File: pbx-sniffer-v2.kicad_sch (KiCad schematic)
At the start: 1 part

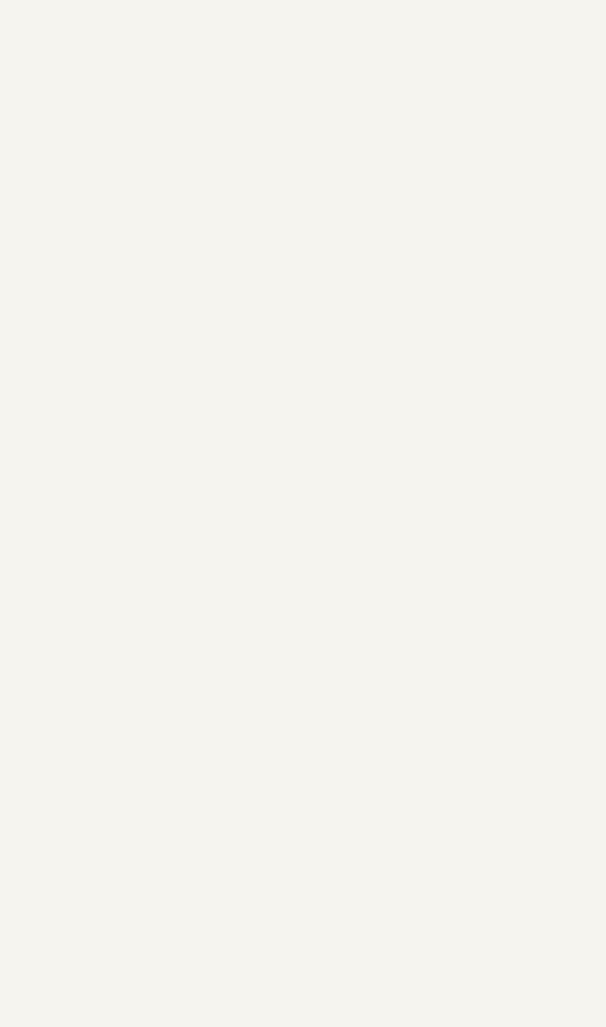
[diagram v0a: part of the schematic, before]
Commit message: first iteration of line control schematic
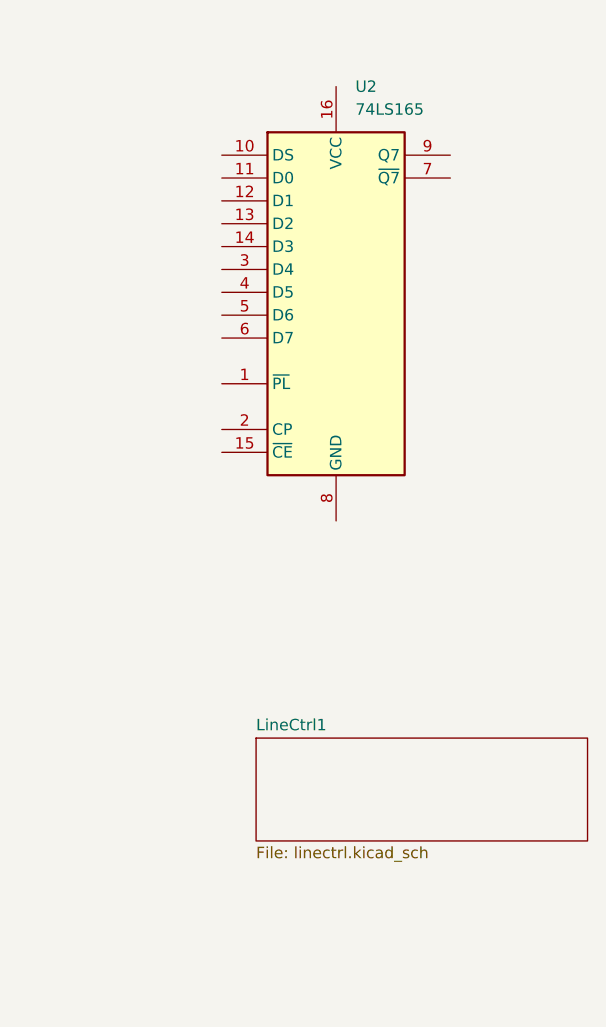
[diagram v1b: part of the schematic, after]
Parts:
- added U2: 74LS165, symbol 74xx:74LS165
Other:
- added sheet LineCtrl1 (linectrl.kicad_sch)
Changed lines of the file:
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@@
+	)
+	(symbol
+		(lib_id "74xx:74LS165")
+		(at 218.44 60.96 0)
+		(unit 1)
+		(body_style 1)
+		(exclude_from_sim no)
+		(in_bom yes)
+		(on_board yes)
+		(in_pos_files yes)
+		(dnp no)
+		(fields_autoplaced yes)
+		(property "Reference" "U2"
+			(at 220.5833 38.1 0)
+			(show_name no)
+			(do_not_autoplace no)
+			(effects
+				(font
+					(size 1.27 1.27)
+				)
+				(justify left)
+			)
+		)
+		(property "Value" "74LS165"
+			(at 220.5833 40.64 0)
+			(show_name no)
+			(do_not_autoplace no)
+			(effects
+				(font
+					(size 1.27 1.27)
+				)
+				(justify left)
+			)
+		)
+		(property "Footprint" ""
+			(at 218.44 60.96 0)
+			(hide yes)
+			(show_name no)
+			(do_not_autoplace no)
+			(effects
+				(font
+					(size 1.27 1.27)
+				)
+			)
+		)
+		(property "Datasheet" "https://www.ti.com/lit/ds/symlink/sn74ls165a.pdf"
+			(at 218.44 60.96 0)
+			(hide yes)
+			(show_name no)
+			(do_not_autoplace no)
+			(effects
+				(font
+					(size 1.27 1.27)
+				)
+			)
+		)
+		(property "Description" "Shift Register 8-bit, parallel load"
+			(at 218.44 60.96 0)
+			(hide yes)
+			(show_name no)
+			(do_not_autoplace no)
+			(effects
+				(font
+					(size 1.27 1.27)
+				)
+			)
+		)
+		(pin "14"
+		)
+		(pin "7"
+		)
+		(pin "3"
+		)
+		(pin "5"
+		)
+		(pin "8"
+		)
+		(pin "4"
+		)
+		(pin "2"
+		)
+		(pin "10"
+		)
+		(pin "6"
+		)
+		(pin "9"
+		)
+		(pin "1"
+		)
+		(pin "12"
+		)
+		(pin "11"
+		)
+		(pin "15"
+		)
+		(pin "16"
+		)
+		(pin "13"
+		)
+		(instances
+			(project "pbx-sniffer-v2"
+				(path "/eb421281-26a1-483f-b39a-0425ec8eb8df"
+					(reference "U2")
+					(unit 1)
+				)
+			)
+		)
 	)
 	(symbol
@@
 				)
 			)
+		)
+	)
+	(sheet
+		(at 209.55 110.49)
+		(size 36.83 11.43)
+		(exclude_from_sim no)
+		(in_bom yes)
+		(on_board yes)
+		(dnp no)
+		(fields_autoplaced yes)
+		(stroke
+			(width 0.1524)
+			(type solid)
+		)
+		(fill
+			(color 0 0 0 0)
+		)
+		(property "Sheetname" "LineCtrl1"
+			(at 209.55 109.7784 0)
+			(show_name no)
+			(do_not_autoplace no)
+			(effects
+				(font
+					(size 1.27 1.27)
+				)
+				(justify left bottom)
+			)
+		)
+		(property "Sheetfile" "linectrl.kicad_sch"
+			(at 209.55 122.5046 0)
+			(show_name no)
+			(do_not_autoplace no)
+			(effects
+				(font
+					(size 1.27 1.27)
+				)
+				(justify left top)
+			)
+		)
+		(instances
+			(project "pbx-sniffer-v2"
+				(path "/eb421281-26a1-483f-b39a-0425ec8eb8df"
+					(page "2")
+				)
+			)

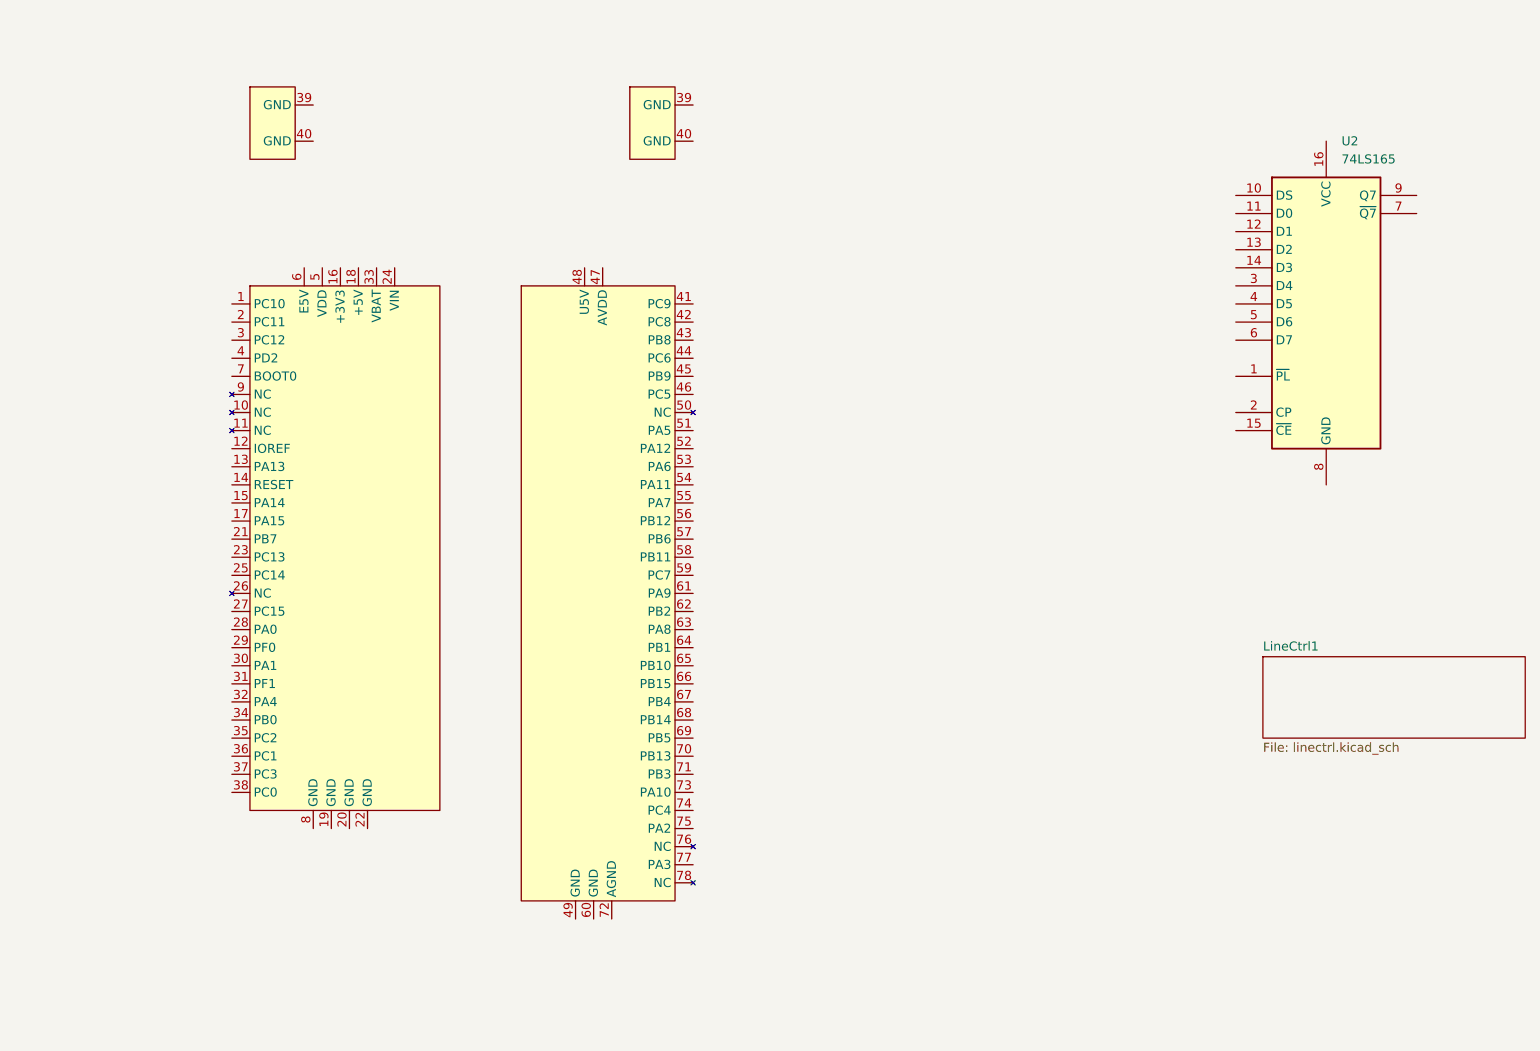
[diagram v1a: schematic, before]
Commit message: add transfer buttons subsheet
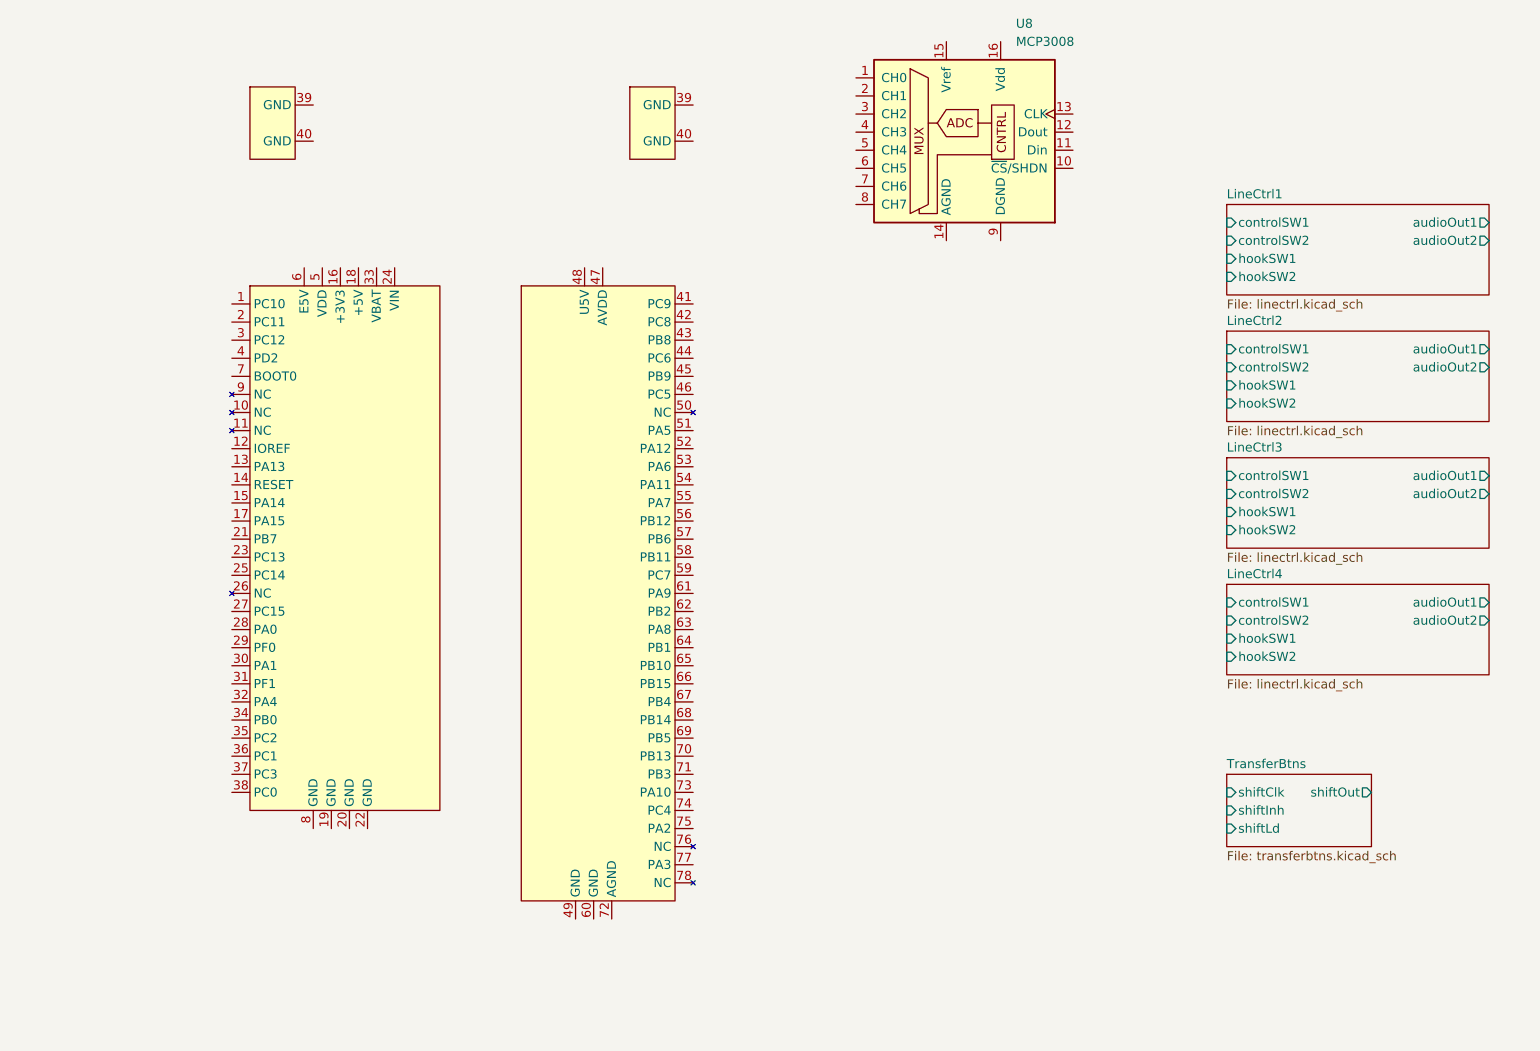
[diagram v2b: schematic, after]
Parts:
- removed U2: 74LS165, symbol 74xx:74LS165
- added U8: MCP3008, symbol Analog_ADC:MCP3008
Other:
- added sheet LineCtrl2 (linectrl.kicad_sch)
- added sheet LineCtrl3 (linectrl.kicad_sch)
- added sheet LineCtrl4 (linectrl.kicad_sch)
- added sheet TransferBtns (transferbtns.kicad_sch)
- sheet LineCtrl1 ports: added audioOut1, audioOut2, controlSW1, controlSW2, hookSW1, hookSW2; removed none

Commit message: start connecting subsheets to main schematic
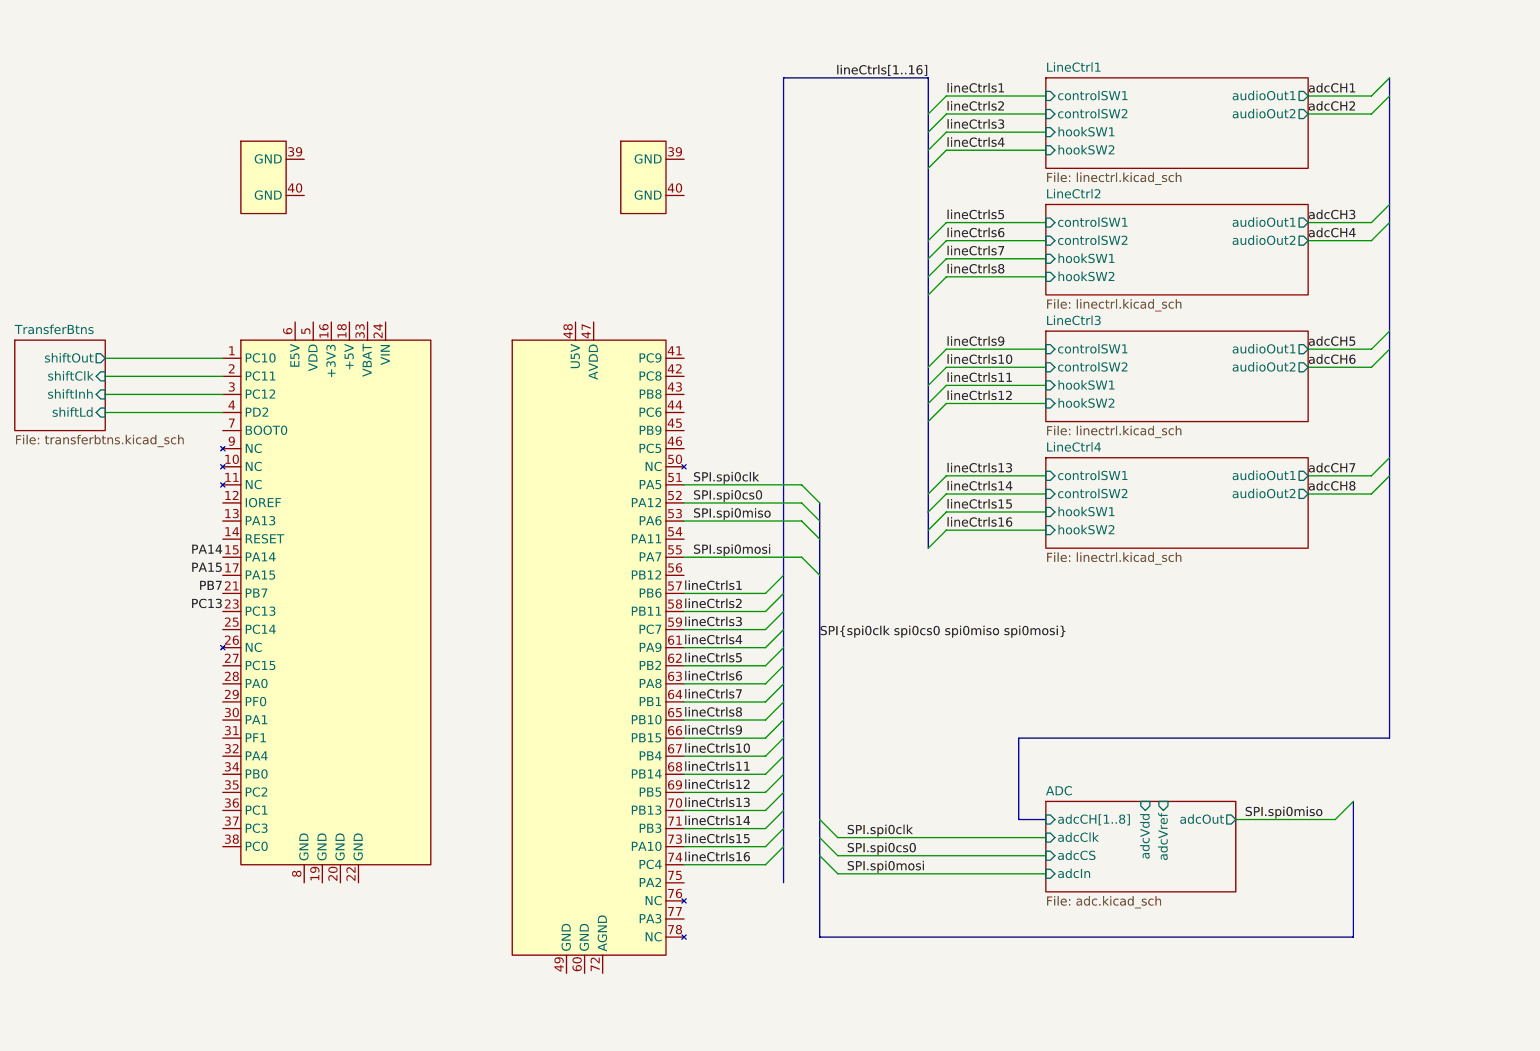
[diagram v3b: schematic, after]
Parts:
- removed U8: MCP3008, symbol Analog_ADC:MCP3008
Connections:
- net TransferBtns/shiftClk: now also U1.2 (PC11)
- net TransferBtns/shiftInh: now also U1.3 (PC12)
- net TransferBtns/shiftLd: now also U1.4 (PD2)
- net TransferBtns/shiftOut: now also U1.1 (PC10)
- net PA14: now reaches U1.15 (PA14)
- net PA15: now reaches U1.17 (PA15)
- net PB7: now reaches U1.21 (PB7)
- net PC13: now reaches U1.23 (PC13)
- net SPI.spi0clk: now reaches U1.51 (PA5)
- net SPI.spi0cs0: now reaches U1.52 (PA12)
- net SPI.spi0miso: now reaches U1.53 (PA6)
- net SPI.spi0mosi: now reaches U1.55 (PA7)
- net lineCtrls1: now reaches U1.57 (PB6)
- net lineCtrls2: now reaches U1.58 (PB11)
- net lineCtrls3: now reaches U1.59 (PC7)
- net lineCtrls4: now reaches U1.61 (PA9)
- net lineCtrls5: now reaches U1.62 (PB2)
- net lineCtrls6: now reaches U1.63 (PA8)
- net lineCtrls7: now reaches U1.64 (PB1)
- net lineCtrls8: now reaches U1.65 (PB10)
- net lineCtrls9: now reaches U1.66 (PB15)
- net lineCtrls10: now reaches U1.67 (PB4)
- net lineCtrls11: now reaches U1.68 (PB14)
- net lineCtrls12: now reaches U1.69 (PB5)
- net lineCtrls13: now reaches U1.70 (PB13)
- net lineCtrls14: now reaches U1.71 (PB3)
- net lineCtrls15: now reaches U1.73 (PA10)
- net lineCtrls16: now reaches U1.74 (PC4)
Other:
- added sheet ADC (adc.kicad_sch)

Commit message: finish schematic capture
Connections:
- net GNDD: now reaches U1.39 (GND)
- net GNDD: now also U1.19 (GND), U1.20 (GND), U1.22 (GND), U1.39 (GND), U1.40 (GND), U1.40 (GND), U1.49 (GND), U1.60 (GND), U1.8 (GND)
- net +3V3: now reaches U1.16 (+3V3)
- net +5V: now reaches U1.18 (+5V)
- net GND: now reaches U1.72 (AGND)
- no-connect marks 0 -> 4
